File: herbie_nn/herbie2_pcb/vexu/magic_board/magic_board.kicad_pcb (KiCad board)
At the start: 2 copper layers, 53.5 x 21 mm, 12 parts, among them J1 4P4C, J2 Conn_ARM_JTAG_SWD_10, U2 ATSAMD21G18A-A, U3 BD33FC0WEFJ, Y1 Crystal

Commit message: updated board
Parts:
- added LED1: LED, LED_SMD:LED_1206_3216Metric, F.Cu at (54.6, 106.5)
- added LED2: LED, LED_SMD:LED_1206_3216Metric, F.Cu at (49.0, 107.0)
- added PWR1: LED, LED_SMD:LED_1206_3216Metric, F.Cu at (30.6, 85.2)
- added R3: 10K, Resistor_SMD:R_1206_3216Metric, F.Cu at (47.0, 102.0)
- added R4: 330, Resistor_SMD:R_1206_3216Metric, F.Cu at (54.5, 102.5)
- added R5: 330, Resistor_SMD:R_1206_3216Metric, F.Cu at (49.0, 104.5)
- added R6: 330, Resistor_SMD:R_1206_3216Metric, F.Cu at (36.0, 85.0)
- added U4: ATSAMD51J19A-A, Package_QFP:TQFP-64_10x10mm_P0.5mm, F.Cu at (69.2, 113.7)
- C1, C2: value C -> 15pF
- turned U2 to 180 degrees
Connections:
- BZ1 pad 2: unconnected-(BZ1---Pad2) -> GND
- C1 pad 1: unconnected-(C1-Pad1) -> GND
- C2 pad 1: unconnected-(C2-Pad1) -> GND
- D1 pad 3: unconnected-(D1-common-Pad3) -> GND
- J1 pad 3: /GND -> GND
- J1 pad 4: /Vcc -> +12V
- J2 pad 1: unconnected-(J2-VTref-Pad1) -> +3.3V
- J2 pad 10: unconnected-(J2-~{RESET}-Pad10) -> /NRESET
- J2 pad 2: unconnected-(J2-SWDIO/TMS-Pad2) -> /SWDIO
- J2 pad 3: Net-(J2-GND-Pad3) -> GND
- J2 pad 4: unconnected-(J2-SWCLK/TCK-Pad4) -> /SWCLK
- J2 pad 5: Net-(J2-GND-Pad3) -> GND
- U1 pad 1: unconnected-(U1-R-Pad1) -> /RX_BRAIN
- U1 pad 2: unconnected-(U1-RE/-Pad2) -> /DIR_BRAIN
- U1 pad 3: unconnected-(U1-DE-Pad3) -> /DIR_BRAIN
- U1 pad 4: unconnected-(U1-D-Pad4) -> /TX_BRAIN
- U1 pad 5: /GND -> GND
- U1 pad 8: unconnected-(U1-Vcc-Pad8) -> +3.3V
- U2 pad 10: unconnected-(U2-PA05-Pad10) -> /RX_BRAIN
- U2 pad 17: unconnected-(U2-VDDIO-Pad17) -> +3.3V
- U2 pad 18: Net-(U2-GND-Pad18) -> GND
- U2 pad 35: Net-(U2-GND-Pad18) -> GND
- U2 pad 36: unconnected-(U2-VDDIO-Pad36) -> +3.3V
- U2 pad 37: unconnected-(U2-PB22-Pad37) -> Net-(U2-PB22)
- U2 pad 38: unconnected-(U2-PB23-Pad38) -> Net-(U2-PB23)
- U2 pad 40: unconnected-(U2-~{RESET}-Pad40) -> /NRESET
- U2 pad 42: Net-(U2-GND-Pad18) -> GND
- U2 pad 44: unconnected-(U2-VDDIN-Pad44) -> +3.3V
- U2 pad 45: unconnected-(U2-PA30-Pad45) -> /SWCLK
- U2 pad 46: unconnected-(U2-PA31-Pad46) -> /SWDIO
- U2 pad 5: unconnected-(U2-GNDANA-Pad5) -> GND
- U2 pad 9: unconnected-(U2-PA04-Pad9) -> /TX_BRAIN
- U3 pad 1: unconnected-(U3-VO-Pad1) -> +3.3V
- U3 pad 3: Net-(U3-GND-Pad3) -> GND
- U3 pad 5: unconnected-(U3-EN-Pad5) -> +12V
- U3 pad 8: unconnected-(U3-VCC-Pad8) -> +12V
- U3 pad 9: Net-(U3-GND-Pad3) -> GND
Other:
- board size 53.5 x 21 mm -> 53.5 x 27.5 mm

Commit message: added SAMD51 and encoder chips
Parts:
- added U5: LS7366R, Package_SO:SOIC-14_3.9x8.7mm_P1.27mm, F.Cu at (48.1, 115.7)
- added U6: LS7366R, Package_SO:SOIC-14_3.9x8.7mm_P1.27mm, F.Cu at (56.5, 115.7)
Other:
- board text added: "Cal Poly Robotics Magic Board v0.1"
- board text removed: "Cal Poly VEXU Magic Board v0.1"

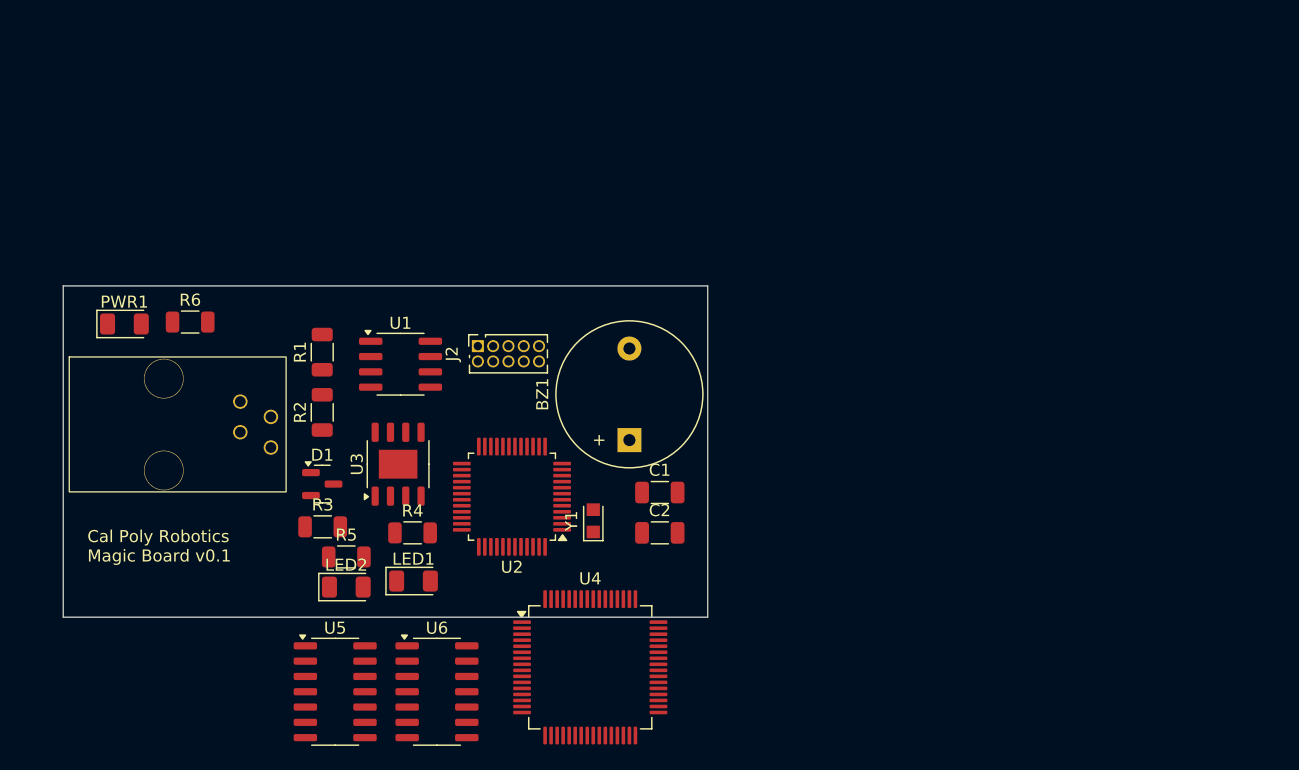
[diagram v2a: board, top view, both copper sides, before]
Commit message: changed to SAMD51J19
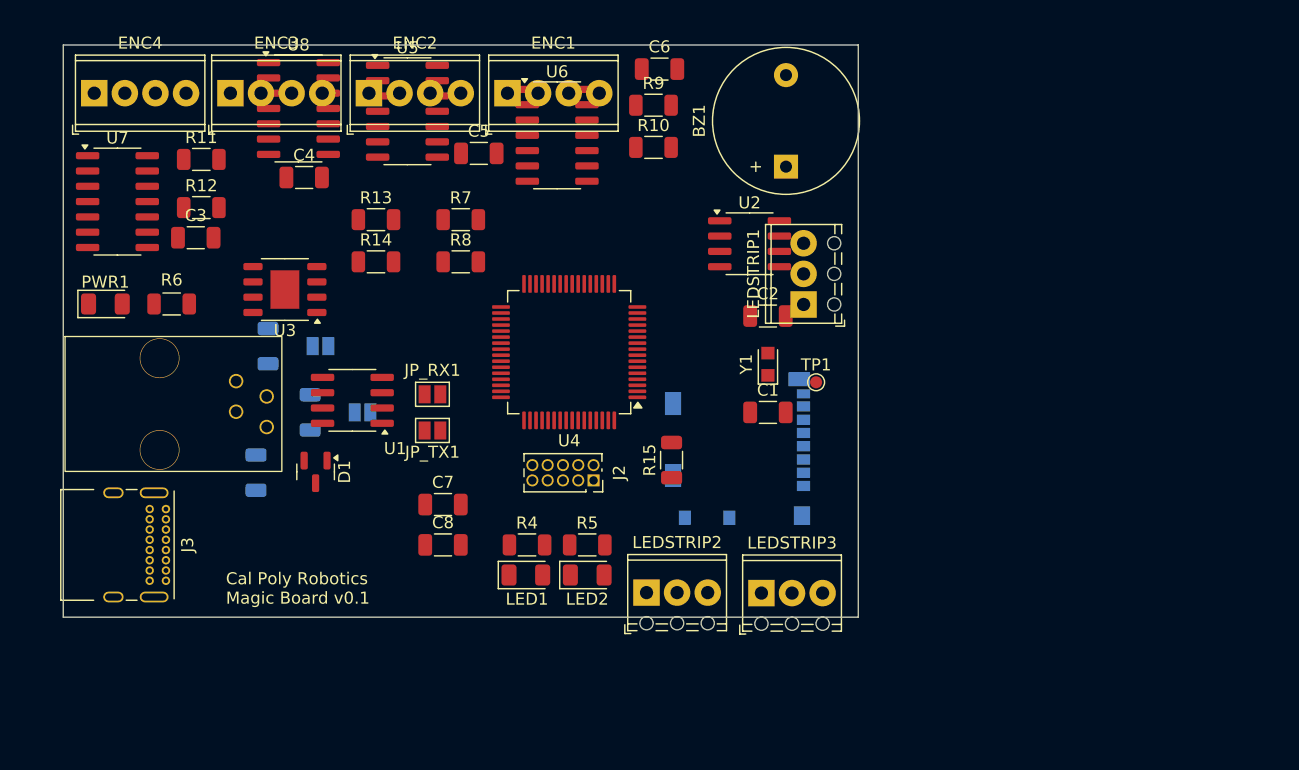
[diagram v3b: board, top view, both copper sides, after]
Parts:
- added C3: C, Capacitor_SMD:C_1206_3216Metric, F.Cu at (36.5, 78.0)
- added C4: C, Capacitor_SMD:C_1206_3216Metric, F.Cu at (45.5, 73.0)
- added C5: C, Capacitor_SMD:C_1206_3216Metric, F.Cu at (60.0, 71.0)
- added C6: C, Capacitor_SMD:C_1206_3216Metric, F.Cu at (75.0, 64.0)
- added C7: 10uF, Capacitor_SMD:C_1206_3216Metric, F.Cu at (57.0, 100.2)
- added C8: 1uF, Capacitor_SMD:C_1206_3216Metric, F.Cu at (57.0, 103.5)
- added ENC1: Screw_Terminal_01x04, TerminalBlock_Phoenix:TerminalBlock_Phoenix_MPT-0,5-4-2.54_1x04_P2.54mm_Horizontal, F.Cu at (62.4, 66.0)
- added ENC2: Screw_Terminal_01x04, TerminalBlock_Phoenix:TerminalBlock_Phoenix_MPT-0,5-4-2.54_1x04_P2.54mm_Horizontal, F.Cu at (50.9, 66.0)
- added ENC3: Screw_Terminal_01x04, TerminalBlock_Phoenix:TerminalBlock_Phoenix_MPT-0,5-4-2.54_1x04_P2.54mm_Horizontal, F.Cu at (39.4, 66.0)
- added ENC4: Screw_Terminal_01x04, TerminalBlock_Phoenix:TerminalBlock_Phoenix_MPT-0,5-4-2.54_1x04_P2.54mm_Horizontal, F.Cu at (28.1, 66.0)
- added J3: USB_C_Receptacle_USB2.0_14P, Connector_USB:USB_C_Receptacle_GCT_USB4085, F.Cu at (34.0, 100.5)
- added J4: Micro_SD_Card, Connector_Card:microSD_HC_Molex_104031-0811, B.Cu at (81.5, 95.5)
- added JP_D+1: Jumper, Jumper:SolderJumper-2_P1.3mm_Open_Pad1.0x1.5mm, B.Cu at (46.9, 87.0)
- added JP_D-1: Jumper, Jumper:SolderJumper-2_P1.3mm_Open_Pad1.0x1.5mm, B.Cu at (50.4, 92.5)
- added JP_RX1: Jumper, Jumper:SolderJumper-2_P1.3mm_Open_Pad1.0x1.5mm, F.Cu at (56.1, 91.0)
- added JP_TX1: Jumper, Jumper:SolderJumper-2_P1.3mm_Open_Pad1.0x1.5mm, F.Cu at (56.1, 94.0)
- added LEDSTRIP1: Screw_Terminal_01x03, TerminalBlock_Phoenix:TerminalBlock_Phoenix_MPT-0,5-3-2.54_1x03_P2.54mm_Horizontal, F.Cu at (87.0, 83.5)
- added LEDSTRIP2: Screw_Terminal_01x03, TerminalBlock_Phoenix:TerminalBlock_Phoenix_MPT-0,5-3-2.54_1x03_P2.54mm_Horizontal, F.Cu at (73.9, 107.5)
- added LEDSTRIP3: Screw_Terminal_01x03, TerminalBlock_Phoenix:TerminalBlock_Phoenix_MPT-0,5-3-2.54_1x03_P2.54mm_Horizontal, F.Cu at (83.5, 107.5)
- added R10: R, Resistor_SMD:R_1206_3216Metric, F.Cu at (74.5, 70.5)
- added R11: R, Resistor_SMD:R_1206_3216Metric, F.Cu at (37.0, 71.5)
- added R12: R, Resistor_SMD:R_1206_3216Metric, F.Cu at (37.0, 75.5)
- added R13: R, Resistor_SMD:R_1206_3216Metric, F.Cu at (51.5, 76.5)
- added R14: R, Resistor_SMD:R_1206_3216Metric, F.Cu at (51.5, 80.0)
- added R15: 10K, Resistor_SMD:R_1206_3216Metric, F.Cu at (76.0, 96.5)
- added R7: R, Resistor_SMD:R_1206_3216Metric, F.Cu at (58.5, 76.5)
- added R8: R, Resistor_SMD:R_1206_3216Metric, F.Cu at (58.5, 80.0)
- added R9: R, Resistor_SMD:R_1206_3216Metric, F.Cu at (74.5, 67.0)
- added TP1: TestPoint, TestPoint:TestPoint_Pad_D1.0mm, F.Cu at (88.0, 90.0)
- added U7: LS7366R, Package_SO:SOIC-14_3.9x8.7mm_P1.27mm, F.Cu at (30.0, 75.0)
- added U8: LS7366R, Package_SO:SOIC-14_3.9x8.7mm_P1.27mm, F.Cu at (45.0, 67.3)
- R1, R2, R3: moved to B.Cu
- U2: value ATSAMD21G18A-A -> AT25SF081-SSHD-X; footprint Package_QFP:TQFP-48_7x7mm_P0.5mm -> Package_SO:SOIC-8_3.9x4.9mm_P1.27mm
- Y1: value Crystal -> 32.768KHz
- moved U5 48.6 mm to (54.1, 67.5)
- moved U6 47.3 mm to (66.5, 69.5)
- moved U2 28.8 mm to (82.5, 78.5), turned to 0 degrees
- moved U4 26.2 mm to (67.5, 87.5), turned to 180 degrees
- moved BZ1 26.2 mm to (85.5, 72.1)
- moved C2 20.1 mm to (84.0, 84.5)
- moved LED2 20.0 mm to (69.0, 106.0)
- moved R5 20.0 mm to (69.0, 103.5)
- moved Y1 19.5 mm to (84.0, 88.5)
- moved U3 17.3 mm to (43.9, 82.3), turned to 180 degrees
- moved J2 14.7 mm to (69.5, 98.1), turned to -90 degrees
- moved C1 11.2 mm to (84.0, 92.5)
- moved R4 9.55 mm to (64.0, 103.5)
- moved LED1 9.34 mm to (63.9, 106.0)
- moved R3 7.14 mm to (41.5, 97.5), turned to -90 degrees
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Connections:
- C1 pad 2: Net-(U2-PA00) -> Net-(U4-PA00)
- C2 pad 2: Net-(U2-PA01) -> Net-(U4-PA01)
- R1 pad 1: Net-(U1-A) -> Net-(JP_D+1-B)
- R2 pad 1: Net-(U1-B) -> Net-(JP_D-1-B)
- R4 pad 2: Net-(U2-PB22) -> unconnected-(R4-Pad2)
- R5 pad 2: Net-(U2-PB23) -> unconnected-(R5-Pad2)
- R6 pad 1: Net-(PWR1-A) -> +3.3V
- R6 pad 2: +3.3V -> Net-(PWR1-A)
- U1 pad 6: Net-(U1-A) -> Net-(JP_D+1-A)
- U1 pad 7: Net-(U1-B) -> Net-(JP_D-1-A)
- U2 pad 1: Net-(U2-PA00) -> /QSPI_CS
- U2 pad 2: Net-(U2-PA01) -> /QSPI_DATA1
- U2 pad 3: unconnected-(U2-PA02-Pad3) -> /QSPI_DATA2
- U2 pad 4: unconnected-(U2-PA03-Pad4) -> GND
- U2 pad 5: GND -> /QSPI_DATA0
- U2 pad 6: unconnected-(U2-VDDANA-Pad6) -> /QSPI_SCK
- U2 pad 7: unconnected-(U2-PB08-Pad7) -> /QSPI_DATA3
- U2 pad 8: unconnected-(U2-PB09-Pad8) -> +3.3V
- U4 pad 1: unconnected-(U4-PA00-Pad1) -> Net-(U4-PA00)
- U4 pad 17: unconnected-(U4-PA08-Pad17) -> /QSPI_DATA0
- U4 pad 18: unconnected-(U4-PA09-Pad18) -> /QSPI_DATA1
- U4 pad 19: unconnected-(U4-PA10-Pad19) -> /QSPI_DATA2
- U4 pad 2: unconnected-(U4-PA01-Pad2) -> Net-(U4-PA01)
- U4 pad 20: unconnected-(U4-PA11-Pad20) -> /QSPI_DATA3
- U4 pad 21: unconnected-(U4-VDDIOB-Pad21) -> +3.3V
- U4 pad 22: Net-(U4-GND-Pad22) -> GND
- U4 pad 23: unconnected-(U4-PB10-Pad23) -> /QSPI_SCK
- U4 pad 24: unconnected-(U4-PB11-Pad24) -> /QSPI_CS
- U4 pad 26: unconnected-(U4-PB13-Pad26) -> /SCK
- U4 pad 27: unconnected-(U4-PB14-Pad27) -> /MISO
- U4 pad 28: unconnected-(U4-PB15-Pad28) -> /MOSI
- U4 pad 29: unconnected-(U4-PA12-Pad29) -> /SDA
- U4 pad 30: unconnected-(U4-PA13-Pad30) -> /SCL
- U4 pad 33: Net-(U4-GND-Pad22) -> GND
- U4 pad 34: unconnected-(U4-VDDIO-Pad34) -> +3.3V
- U4 pad 45: unconnected-(U4-PA24-Pad45) -> /D-
- U4 pad 46: unconnected-(U4-PA25-Pad46) -> /D+
- U4 pad 47: Net-(U4-GND-Pad22) -> GND
- U4 pad 48: unconnected-(U4-VDDIO-Pad48) -> +3.3V
- U4 pad 51: unconnected-(U4-PA27-Pad51) -> /DIR_BRAIN
- U4 pad 52: unconnected-(U4-~{RESET}-Pad52) -> /NRESET
- U4 pad 54: Net-(U4-GND-Pad22) -> GND
- U4 pad 56: unconnected-(U4-VDDIO-Pad56) -> +3.3V
- U4 pad 57: unconnected-(U4-PA30-Pad57) -> /SWCLK
- U4 pad 58: unconnected-(U4-PA31-Pad58) -> /SWDIO
- U4 pad 59: unconnected-(U4-PB30-Pad59) -> Net-(JP_RX1-A)
- U4 pad 60: unconnected-(U4-PB31-Pad60) -> Net-(JP_TX1-A)
- U4 pad 7: unconnected-(U4-GNDANA-Pad7) -> GND
- U5 pad 11: unconnected-(U5-b-Pad11) -> Net-(U5-b)
- U5 pad 12: unconnected-(U5-a-Pad12) -> Net-(U5-a)
- U5 pad 4: unconnected-(U5-ss-Pad4) -> /ENC1_SS
- U5 pad 5: unconnected-(U5-sck-Pad5) -> /SCK
- U5 pad 6: unconnected-(U5-miso-Pad6) -> /MISO
- U5 pad 7: unconnected-(U5-mosi-Pad7) -> /MOSI
- U6 pad 11: unconnected-(U6-b-Pad11) -> Net-(U6-b)
- U6 pad 12: unconnected-(U6-a-Pad12) -> Net-(U6-a)
- U6 pad 4: unconnected-(U6-ss-Pad4) -> /ENC2_SS
- U6 pad 5: unconnected-(U6-sck-Pad5) -> /SCK
- U6 pad 6: unconnected-(U6-miso-Pad6) -> /MISO
- U6 pad 7: unconnected-(U6-mosi-Pad7) -> /MOSI
- Y1 pad 1: Net-(U2-PA00) -> Net-(U4-PA00)
- Y1 pad 2: Net-(U2-PA01) -> Net-(U4-PA01)
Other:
- board size 53.5 x 27.5 mm -> 66 x 47.5 mm

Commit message: updated board
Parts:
- removed R8: R, Resistor_SMD:R_1206_3216Metric
- added C10: C, Capacitor_SMD:C_1206_3216Metric, F.Cu at (67.8, 77.5)
- added C9: C, Capacitor_SMD:C_1206_3216Metric, F.Cu at (57.9, 77.1)
- added H1: MountingHole, MountingHole:MountingHole_3.2mm_M3_DIN965, F.Cu at (92.4, 65.1)
- added H2: MountingHole, MountingHole:MountingHole_3.2mm_M3_DIN965, F.Cu at (28.6, 65.1)
- added H3: MountingHole, MountingHole:MountingHole_3.2mm_M3_DIN965, F.Cu at (28.6, 108.9)
- added H4: MountingHole, MountingHole:MountingHole_3.2mm_M3_DIN965, F.Cu at (92.4, 108.9)
- added J5: Conn_01x04_Pin, Connector_PinHeader_2.54mm:PinHeader_1x04_P2.54mm_Vertical, F.Cu at (80.6, 80.9)
- added R16: R, Resistor_SMD:R_1206_3216Metric, B.Cu at (46.2, 108.3)
- added R17: R, Resistor_SMD:R_1206_3216Metric, B.Cu at (36.4, 104.5)
- added U10: SN74LVC245APW, Package_SO:TSSOP-20_4.4x6.5mm_P0.65mm, B.Cu at (60.3, 106.3)
- added U11: 74HC14, Package_SO:TSSOP-14_4.4x5mm_P0.65mm, F.Cu at (50.6, 75.4)
- added U9: SN74LVC245APW, Package_SO:TSSOP-20_4.4x6.5mm_P0.65mm, B.Cu at (60.0, 67.6)
- added Y2: 20MHz, Crystal:Crystal_SMD_2012-2Pin_2.0x1.2mm_HandSoldering, F.Cu at (59.5, 73.2)
- BZ1: footprint Buzzer_Beeper:Buzzer_12x9.5RM7.6 -> Buzzer_Beeper:Buzzer_TDK_PS1240P02BT_D12.2mm_H6.5mm
- C3, C4, C5, C6, C7, C8, JP_RX1, JP_TX1, R10, R11, R12, R13, R14, R4, R5, R6, R9: moved to B.Cu
- J4: value Micro_SD_Card -> Conn_01x04_Pin; footprint Connector_Card:microSD_HC_Molex_104031-0811 -> Connector_PinHeader_2.54mm:PinHeader_1x04_P2.54mm_Vertical; moved to F.Cu
- R7: value R -> 1M
- moved ENC3 63.7 mm to (86.9, 108.4), turned to 180 degrees
- moved LEDSTRIP2 58.2 mm to (29.1, 70.4), turned to -90 degrees
- moved U7 48.2 mm to (66.4, 106.6)
- moved ENC4 44.5 mm to (41.5, 108.4), turned to 180 degrees
- moved R13 43.3 mm to (84.4, 104.6), turned to 90 degrees
- moved U8 40.7 mm to (55.3, 106.7)
- moved C6 39.5 mm to (58.0, 99.6), turned to 90 degrees
- moved R14 37.5 mm to (76.0, 108.4), turned to 90 degrees
- moved C8 32.1 mm to (38.7, 77.1), turned to 180 degrees
- moved C7 31.6 mm to (38.7, 74.4), turned to 180 degrees
- moved C5 31.6 mm to (68.8, 101.3), turned to -90 degrees
- moved C4 20.8 mm to (66.2, 74.7), turned to -90 degrees
- moved PWR1 19.0 mm to (39.8, 99.1), turned to 180 degrees
- moved C3 17.5 mm to (53.7, 74.6), turned to -90 degrees
- moved R12 16.6 mm to (50.6, 66.0), turned to -90 degrees
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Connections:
- BZ1 pad 1: unconnected-(BZ1-+-Pad1) -> /BUZ_PIN
- ENC1 pad 2: unconnected-(ENC1-Pin_2-Pad2) -> /A1_IN
- ENC1 pad 3: unconnected-(ENC1-Pin_3-Pad3) -> /B1_IN
- ENC2 pad 2: unconnected-(ENC2-Pin_2-Pad2) -> /A2_IN
- ENC2 pad 3: unconnected-(ENC2-Pin_3-Pad3) -> /B2_IN
- ENC3 pad 2: unconnected-(ENC3-Pin_2-Pad2) -> /A3_IN
- ENC3 pad 3: unconnected-(ENC3-Pin_3-Pad3) -> /B3_IN
- ENC4 pad 2: unconnected-(ENC4-Pin_2-Pad2) -> /A4_IN
- ENC4 pad 3: unconnected-(ENC4-Pin_3-Pad3) -> /B4_IN
- LEDSTRIP1 pad 1: unconnected-(LEDSTRIP1-Pin_1-Pad1) -> GND
- LEDSTRIP1 pad 2: unconnected-(LEDSTRIP1-Pin_2-Pad2) -> /LED_SIG1
- LEDSTRIP1 pad 3: unconnected-(LEDSTRIP1-Pin_3-Pad3) -> +12V
- LEDSTRIP2 pad 1: unconnected-(LEDSTRIP2-Pin_1-Pad1) -> GND
- LEDSTRIP2 pad 2: unconnected-(LEDSTRIP2-Pin_2-Pad2) -> /LED_SIG2
- LEDSTRIP2 pad 3: unconnected-(LEDSTRIP2-Pin_3-Pad3) -> +12V
- LEDSTRIP3 pad 1: unconnected-(LEDSTRIP3-Pin_1-Pad1) -> GND
- LEDSTRIP3 pad 2: unconnected-(LEDSTRIP3-Pin_2-Pad2) -> /LED_SIG3
- LEDSTRIP3 pad 3: unconnected-(LEDSTRIP3-Pin_3-Pad3) -> +12V
- R10 pad 1: Net-(U6-b) -> /B1_IN
- R10 pad 2: unconnected-(R10-Pad2) -> Net-(U9-A2)
- R11 pad 1: Net-(U7-a) -> /A2_IN
- R11 pad 2: unconnected-(R11-Pad2) -> Net-(U9-A3)
- R12 pad 1: Net-(U7-b) -> /B2_IN
- R12 pad 2: unconnected-(R12-Pad2) -> Net-(U9-A4)
- R13 pad 1: Net-(U8-a) -> /A3_IN
- R13 pad 2: unconnected-(R13-Pad2) -> Net-(U10-A5)
- R14 pad 1: Net-(U8-b) -> /B3_IN
- R14 pad 2: unconnected-(R14-Pad2) -> Net-(U10-A6)
- R7 pad 1: Net-(U5-a) -> Net-(U5-fcki)
- R7 pad 2: unconnected-(R7-Pad2) -> /EN_CLK
- R9 pad 1: Net-(U6-a) -> /A1_IN
- R9 pad 2: unconnected-(R9-Pad2) -> Net-(U9-A1)
- U4 pad 10: unconnected-(U4-PB07-Pad10) -> /ENC4_SS
- U4 pad 11: unconnected-(U4-PB08-Pad11) -> /BUZ_PIN
- U4 pad 13: unconnected-(U4-PA04-Pad13) -> /SERCOM0.0
- U4 pad 14: unconnected-(U4-PA05-Pad14) -> /SERCOM0.1
- U4 pad 15: unconnected-(U4-PA06-Pad15) -> /SERCOM0.2
- U4 pad 16: unconnected-(U4-PA07-Pad16) -> /SERCOM0.3
- U4 pad 3: unconnected-(U4-PA02-Pad3) -> /DAC_OUT0
- U4 pad 35: unconnected-(U4-PA16-Pad35) -> /SERCOM1.0
- U4 pad 36: unconnected-(U4-PA17-Pad36) -> /SERCOM1.1
- U4 pad 37: unconnected-(U4-PA18-Pad37) -> /SERCOM1.2
- U4 pad 38: unconnected-(U4-PA19-Pad38) -> /SERCOM1.3
- U4 pad 5: unconnected-(U4-PB04-Pad5) -> /ENC1_SS
- U4 pad 6: unconnected-(U4-PB05-Pad6) -> /ENC2_SS
- U4 pad 62: unconnected-(U4-PB01-Pad62) -> /LED_SIG3
- U4 pad 63: unconnected-(U4-PB02-Pad63) -> /LED_SIG2
- U4 pad 64: unconnected-(U4-PB03-Pad64) -> /LED_SIG1
- U4 pad 9: unconnected-(U4-PB06-Pad9) -> /ENC3_SS
- U5 pad 1: unconnected-(U5-fcko-Pad1) -> /EN_CLK
- U5 pad 11: Net-(U5-b) -> /B1
- U5 pad 12: Net-(U5-a) -> /A1
- U5 pad 2: unconnected-(U5-fcki-Pad2) -> Net-(U5-fcki)
- U6 pad 11: Net-(U6-b) -> /B2
- U6 pad 12: Net-(U6-a) -> /A2
- U6 pad 2: unconnected-(U6-fcki-Pad2) -> /OUT_CLK
- U7 pad 11: Net-(U7-b) -> /B3
- U7 pad 12: Net-(U7-a) -> /A3
- U7 pad 2: unconnected-(U7-fcki-Pad2) -> /OUT_CLK
- U8 pad 11: Net-(U8-b) -> /B4
- U8 pad 12: Net-(U8-a) -> /A4
- U8 pad 2: unconnected-(U8-fcki-Pad2) -> /OUT_CLK
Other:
- board size 66 x 47.5 mm -> 70 x 50 mm
- board text removed: "Cal Poly Robotics Magic Board v0.1"
